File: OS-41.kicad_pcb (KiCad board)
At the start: 4 copper layers, 26.1 x 54.5 mm, 67 parts, among them J2 Conn_01x02_Pin, J3 Conn_01x02_Pin, J4 Conn_Coaxial, J6 Conn_01x04_Pin, J8 Conn_01x02_Pin, J9 Conn_01x02_Pin, U2 SI4432-B1-FMR, U3 MCP1640x-xCHY, U4 ATGM336H-5N31, U6 BMP390L, U7 STM32F411CEUx, Y1 Crystal_GND24, Y2 Crystal, Y3 Crystal_GND24

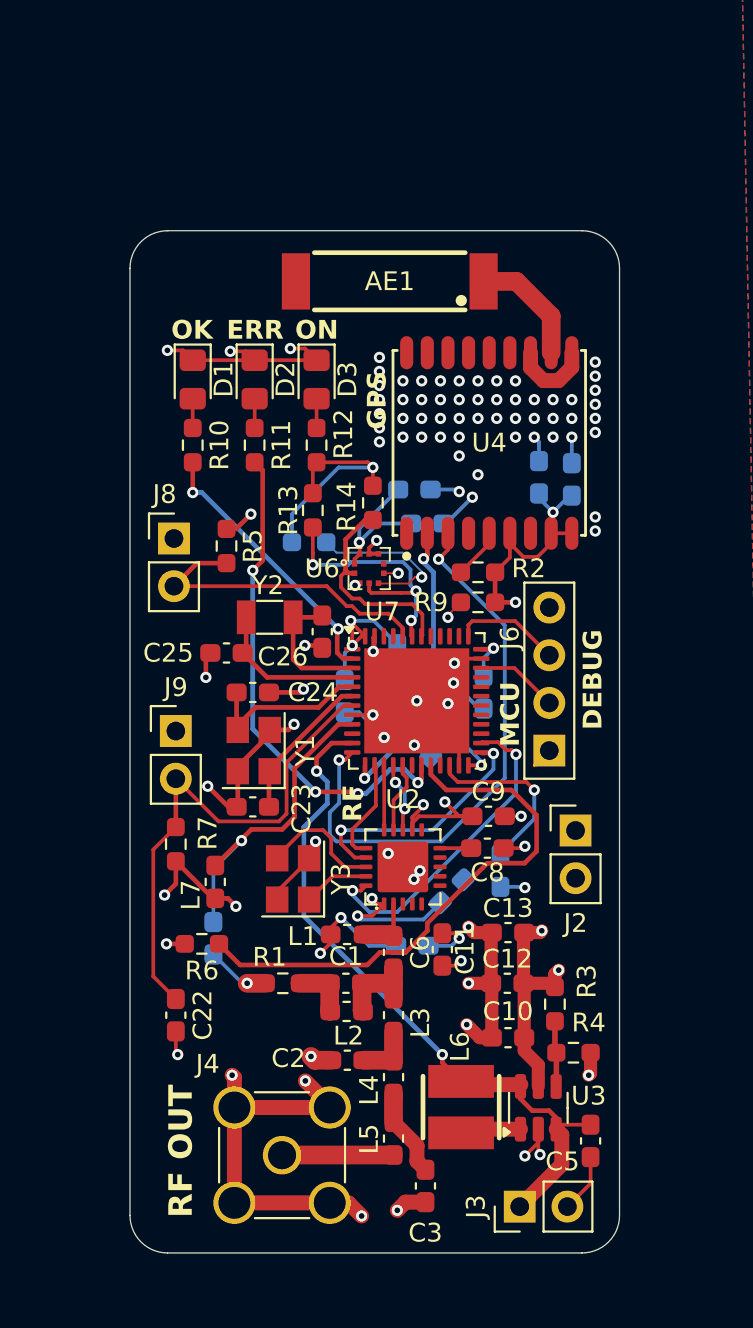
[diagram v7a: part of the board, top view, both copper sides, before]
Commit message: Change GPS antenna + routing fixes
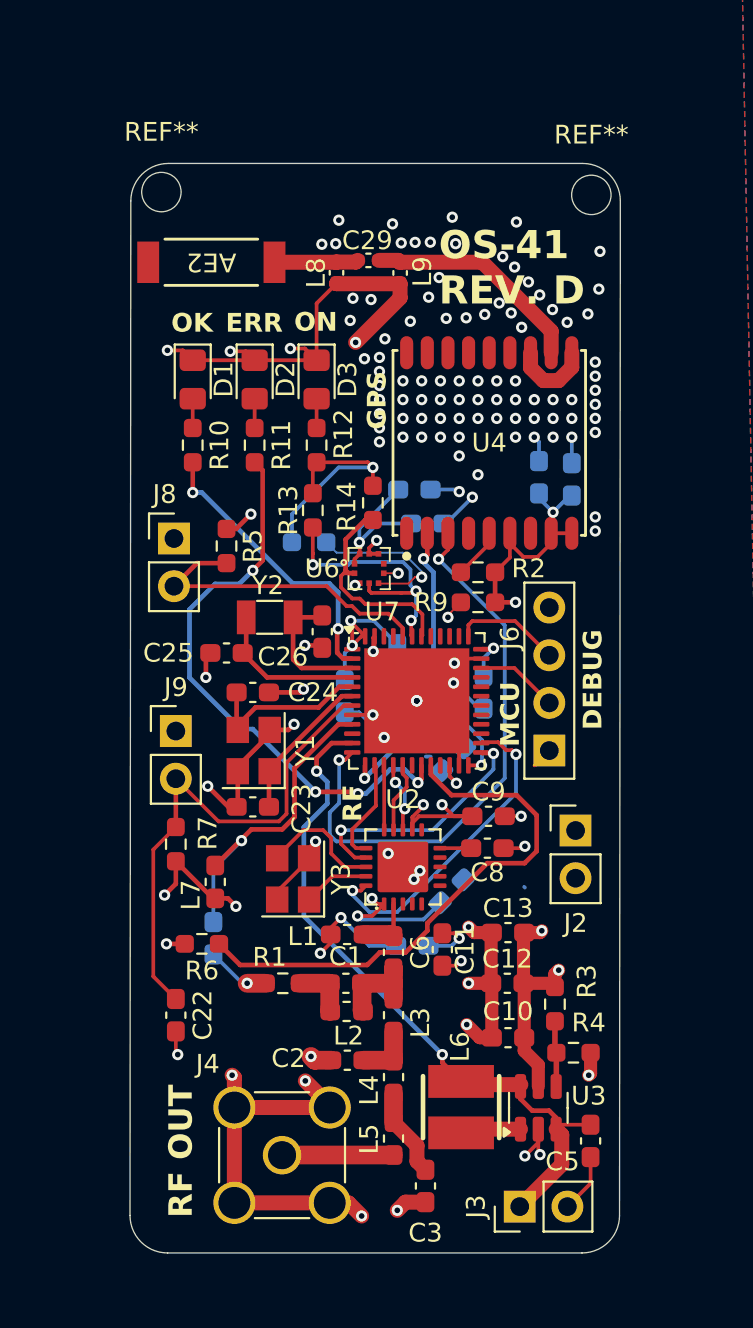
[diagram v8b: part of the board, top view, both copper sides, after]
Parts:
- removed AE1: Antenna, libsos41:ANT-SMD_L10.0-W3.0
- added AE2: 1575AT43A0040, centdir:ANT_1575AT_JOT, F.Cu at (128.8, 81.7)
- added C29: 1.5pF, Capacitor_SMD:C_0402_1005Metric_Pad0.74x0.62mm_HandSolder, F.Cu at (137.2, 81.6)
- added L8: 3.9 nH, Inductor_SMD:L_0402_1005Metric_Pad0.77x0.64mm_HandSolder, F.Cu at (135.5, 82.2)
- added L9: 3.9 nH, Inductor_SMD:L_0402_1005Metric_Pad0.77x0.64mm_HandSolder, F.Cu at (138.8, 82.2)
- added REF**: MountingHole_2.1mm, MountingHole:MountingHole_2.1mm, F.Cu at (149.0, 78.1)
- added REF**: MountingHole_2.1mm, MountingHole:MountingHole_2.1mm, F.Cu at (126.1, 77.9)
- moved C21 6.45 mm to (141.7, 108.2), turned to 45 degrees
- moved C18 0.82 mm to (140.9, 106.6)
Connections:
- U4 pad 11: GPS_ANT -> Net-(U4-RF_IN)
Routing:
- net Net-(U4-RF_IN): track 0.00 -> 11.9 mm
- net GND: track 147.3 -> 155.5 mm, vias 95 -> 127
- net Net-(U7-VCAP1): track 9.50 -> 2.16 mm
- net GPS_ANT: track 6.32 -> 0.00 mm
- net Net-(AE2-A): track 0.00 -> 4.48 mm
- net LED_ERR: track 26.7 -> 30.6 mm
- net LED_OK: track 14.7 -> 15.9 mm
- net VCC: track 112.7 -> 113.2 mm
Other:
- board size 26.1 x 54.5 mm -> 26.1 x 58.1 mm
- board text added: "To infinity and beyond!"
- board text removed: "STM32+GPS+Radio"
